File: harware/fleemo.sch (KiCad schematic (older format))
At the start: 33 parts, among them P1 CONN_01X02, Q1 STD2HNK60Z-1

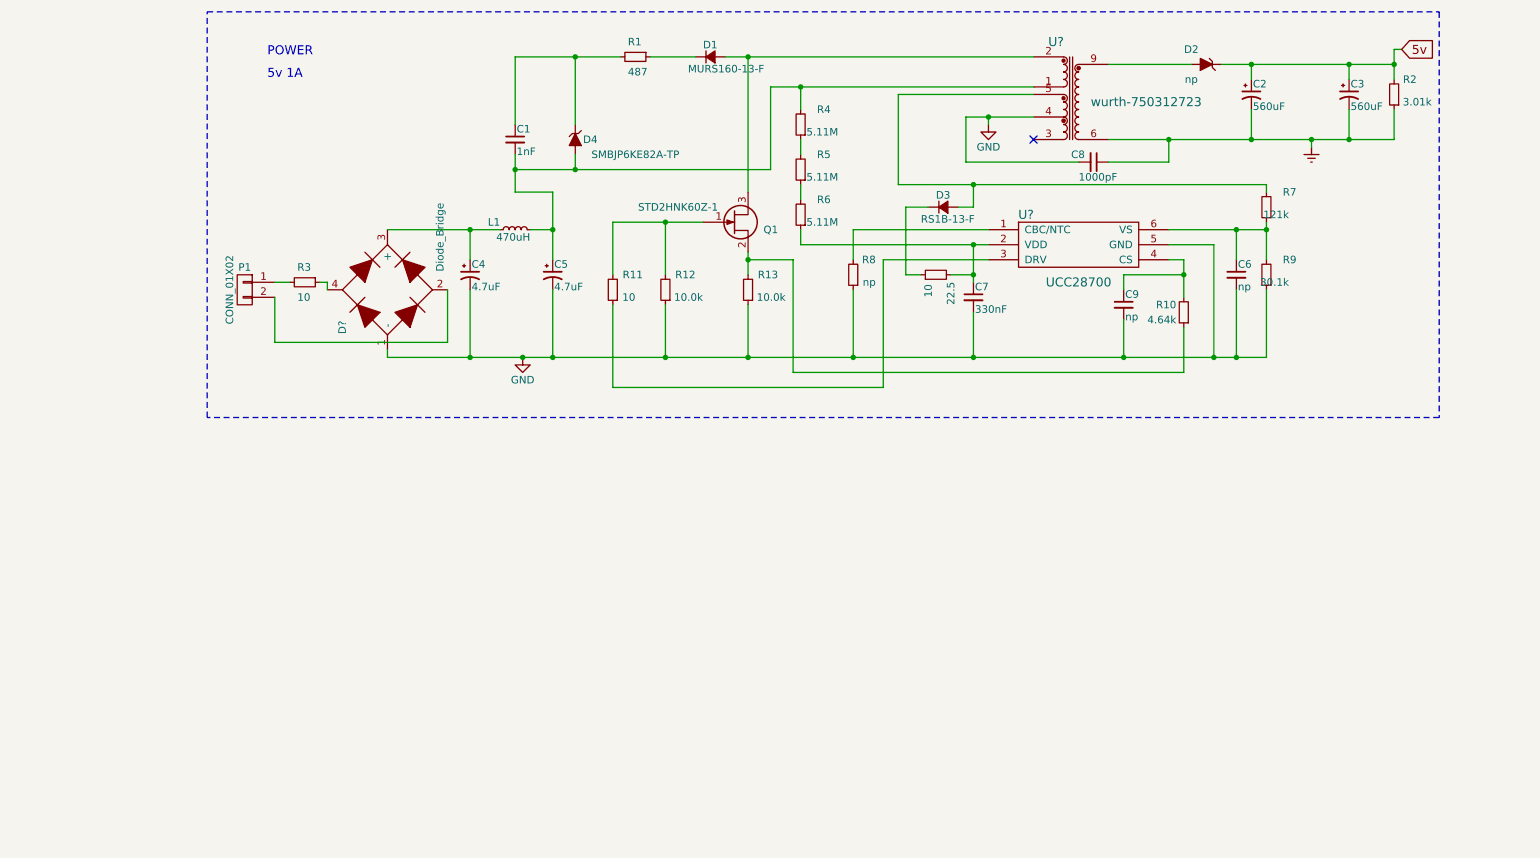
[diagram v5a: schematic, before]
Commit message: add stepdown circuit
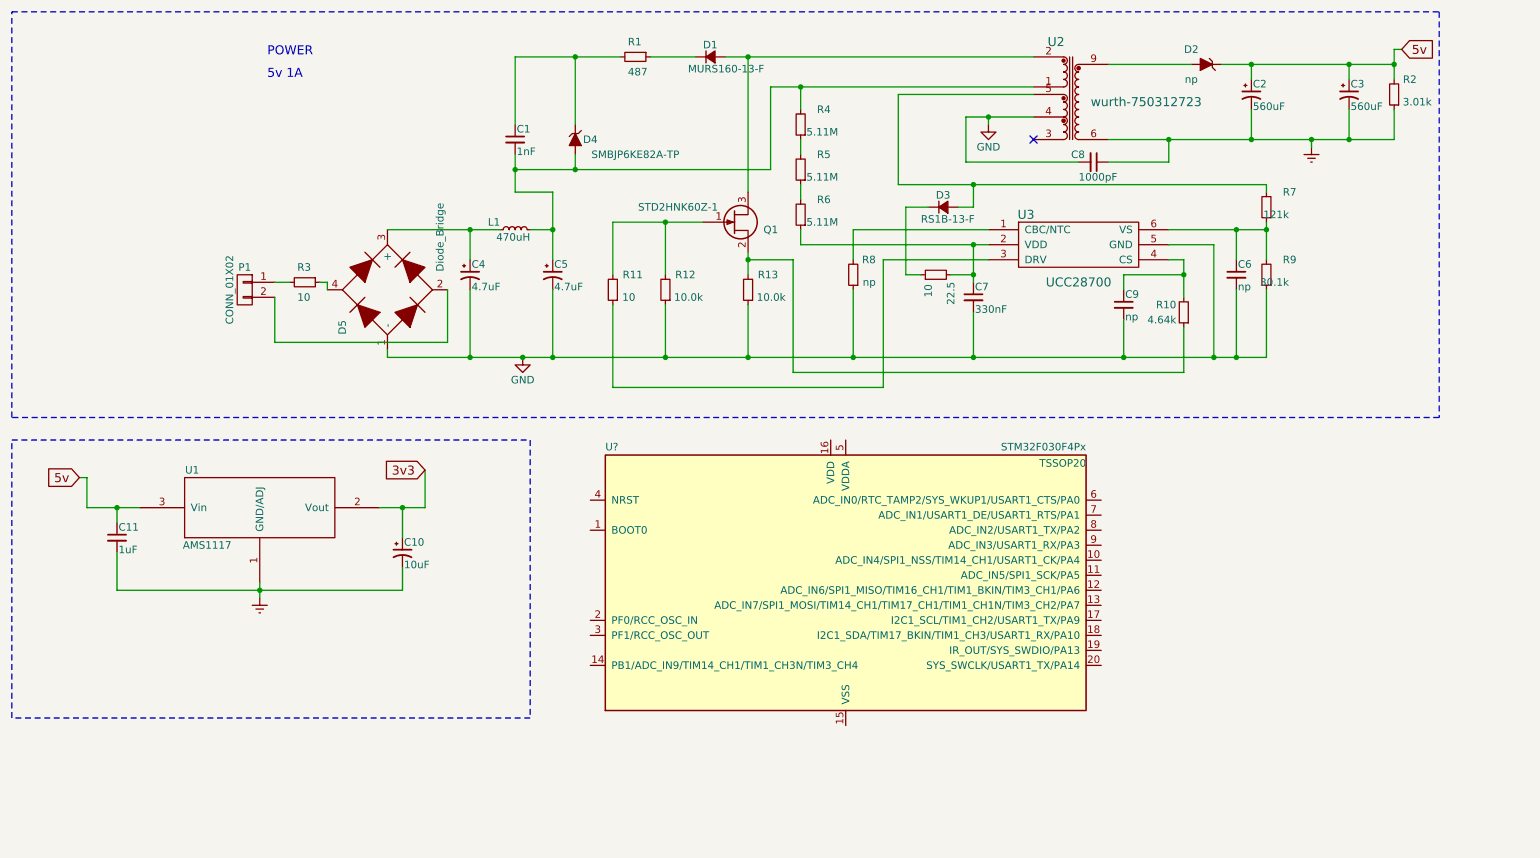
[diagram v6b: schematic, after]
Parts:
- added C10: 10uF, symbol CP1_Small
- added C11: 1uF, symbol C_Small
- added U1: AMS1117, symbol AMS1117
- added U?: STM32F030F4Px, TSSOP20, symbol STM32F030F4Px
- gave numbers to parts that had none: 3
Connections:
- net 5v: now also C11.1, U1.3 (Vin)
- net Earth: now also C10.2, C11.2, U1.1 (GND/ADJ)
- new net 3v3: C10.1, U1.2 (Vout)
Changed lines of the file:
@@
 LIBS:wurth-750312723
 LIBS:UCC28700
+LIBS:stm32
+LIBS:Power_Management
+LIBS:AMS1117
 LIBS:fleemo-cache
 EELAYER 25 0
@@
 $EndComp
 $Comp
-L GND #PWR01
+L GND #PWR2
 U 1 1 578589FE
 P 4500 3100
-F 0 "#PWR01" H 4500 2850 50  0001 C CNN
+F 0 "#PWR2" H 4500 2850 50  0001 C CNN
 F 1 "GND" H 4500 2950 50  0000 C CNN
 F 2 "" H 4500 3100 50  0000 C CNN
@@
 $EndComp
 $Comp
-L Earth #PWR05
+L Earth #PWR4
 U 1 1 578722E6
 P 9750 1700
-F 0 "#PWR05" H 9750 1450 50  0001 C CNN
+F 0 "#PWR4" H 9750 1450 50  0001 C CNN
 F 1 "Earth" H 9750 1550 50  0001 C CNN
 F 2 "" H 9750 1700 50  0000 C CNN
@@
 $EndComp
 $Comp
-L wurth-750312723 U?
+L wurth-750312723 U2
 U 1 1 578D71AD
 P 8150 1900
-F 0 "U?" H 8050 2800 60  0000 C CNN
+F 0 "U2" H 8050 2800 60  0000 C CNN
 F 1 "wurth-750312723" H 8650 2400 60  0000 C CNN
 F 2 "" H 8150 1900 60  0000 C CNN
@@
 $EndComp
 $Comp
-L UCC28700 U?
+L UCC28700 U3
 U 1 1 578EB042
 P 8200 2600
-F 0 "U?" H 7850 3050 60  0000 C CNN
+F 0 "U3" H 7850 3050 60  0000 C CNN
 F 1 "UCC28700" H 8200 2600 60  0000 C CNN
 F 2 "" H 8200 2600 60  0000 C CNN
@@
 $EndComp
 $Comp
-L GND #PWR?
+L GND #PWR3
 U 1 1 578EBE22
 P 7600 1550
-F 0 "#PWR?" H 7600 1300 50  0001 C CNN
+F 0 "#PWR3" H 7600 1300 50  0001 C CNN
 F 1 "GND" H 7600 1400 50  0000 C CNN
 F 2 "" H 7600 1550 50  0000 C CNN
@@
 	4700 3100 4700 2650
 Wire Wire Line
-	5100 2200 5450 2200
-Wire Wire Line
-	5450 2200 5700 2200
+	5100 2200 5700 2200
 Connection ~ 4500 3100
 Wire Wire Line
@@
 	4150 2250 4150 2450
 Wire Wire Line
-	4700 2000 4700 2250
-Wire Wire Line
-	4700 2250 4700 2450
+	4700 2000 4700 2450
 Wire Wire Line
 	4700 2250 4550 2250
@@
 	4450 2000 4700 2000
 Wire Wire Line
-	4450 1750 4450 1850
-Wire Wire Line
-	4450 1850 4450 2000
+	4450 1750 4450 2000
 Wire Wire Line
 	4450 1550 4450 1100
 Wire Wire Line
-	4450 1100 4850 1100
-Wire Wire Line
-	4850 1100 5150 1100
-Wire Wire Line
-	4450 1850 4850 1850
-Wire Wire Line
-	4850 1850 6150 1850
+	4450 1100 5150 1100
+Wire Wire Line
+	4450 1850 6150 1850
 Wire Wire Line
 	4850 1850 4850 1750
@@
 	5350 1100 5650 1100
 Wire Wire Line
-	5850 1100 6000 1100
-Wire Wire Line
-	6000 1100 7900 1100
+	5850 1100 7900 1100
 Wire Wire Line
 	6000 1100 6000 2000
@@
 	5450 2550 5450 2200
 Wire Wire Line
-	6000 2400 6000 2450
-Wire Wire Line
-	6000 2450 6000 2550
+	6000 2400 6000 2550
 Wire Wire Line
 	6000 3100 6000 2750
@@
 	6350 1450 6350 1300
 Wire Wire Line
-	6150 1300 6350 1300
-Wire Wire Line
-	6350 1300 7900 1300
+	6150 1300 7900 1300
 Wire Wire Line
 	6350 1650 6350 1750
@@
 	6350 2250 6350 2350
 Wire Wire Line
-	6350 2350 7500 2350
-Wire Wire Line
-	7500 2350 7600 2350
+	6350 2350 7600 2350
 Wire Wire Line
 	5100 2550 5100 2200
@@
 	7000 1350 7000 1950
 Wire Wire Line
-	7000 1950 7500 1950
-Wire Wire Line
-	7500 1950 9450 1950
+	7000 1950 9450 1950
 Wire Wire Line
 	9450 1950 9450 2000
 Wire Wire Line
-	9450 2200 9450 2250
-Wire Wire Line
-	9450 2250 9450 2450
+	9450 2200 9450 2450
 Wire Wire Line
 	9450 3100 9450 2650
@@
 $EndComp
 Wire Wire Line
-	7500 2350 7500 2550
-Wire Wire Line
-	7500 2550 7500 2600
+	7500 2350 7500 2600
 Connection ~ 7500 2350
 Wire Wire Line
@@
 Connection ~ 7500 1950
 Wire Wire Line
-	8800 2250 9250 2250
-Wire Wire Line
-	9250 2250 9450 2250
+	8800 2250 9450 2250
 Connection ~ 9450 2250
 $Comp
@@
 	8800 2450 8900 2450
 Wire Wire Line
-	8900 2450 8900 2550
-Wire Wire Line
-	8900 2550 8900 2700
+	8900 2450 8900 2700
 Wire Wire Line
 	8900 2900 8900 3200
@@
 	8800 2350 9100 2350
 Wire Wire Line
-	9100 2350 9100 3100
+	9100 3100 9100 2350
 Connection ~ 9100 3100
 $Comp
@@
 $EndComp
 Wire Wire Line
-	9150 1150 9350 1150
-Wire Wire Line
-	9350 1150 10000 1150
-Wire Wire Line
-	10000 1150 10300 1150
+	9150 1150 10300 1150
 Wire Wire Line
 	9350 1150 9350 1250
 Wire Wire Line
-	8400 1650 8800 1650
-Wire Wire Line
-	8800 1650 9350 1650
-Wire Wire Line
-	9350 1650 9750 1650
-Wire Wire Line
-	9750 1650 10000 1650
-Wire Wire Line
-	10000 1650 10300 1650
+	8400 1650 10300 1650
 Wire Wire Line
 	9350 1650 9350 1450
@@
 $EndComp
 Wire Wire Line
-	10300 1050 10300 1150
-Wire Wire Line
-	10300 1150 10300 1250
+	10300 1050 10300 1250
 Connection ~ 10000 1150
 Wire Wire Line
@@
 $EndComp
 Wire Wire Line
-	7900 1500 7600 1500
-Wire Wire Line
-	7600 1500 7450 1500
+	7450 1500 7900 1500
 Wire Wire Line
 	7450 1500 7450 1800
@@
 NoConn ~ 7900 1650
 $Comp
-L Diode_Bridge D?
+L Diode_Bridge D5
 U 1 1 578EFF8B
 P 3600 2650
-F 0 "D?" H 3350 2950 50  0000 C CNN
+F 0 "D5" H 3350 2950 50  0000 C CNN
 F 1 "Diode_Bridge" H 3950 2300 50  0000 C CNN
 F 2 "" H 3600 2650 50  0000 C CNN
@@
 $EndComp
 Wire Wire Line
-	3600 2250 4150 2250
-Wire Wire Line
-	4150 2250 4350 2250
-Wire Wire Line
-	3600 3100 4150 3100
-Wire Wire Line
-	4150 3100 4500 3100
-Wire Wire Line
-	4500 3100 4700 3100
-Wire Wire Line
-	4700 3100 5450 3100
-Wire Wire Line
-	5450 3100 6000 3100
-Wire Wire Line
-	6000 3100 6700 3100
-Wire Wire Line
-	6700 3100 7500 3100
-Wire Wire Line
-	7500 3100 8500 3100
-Wire Wire Line
-	8500 3100 9100 3100
-Wire Wire Line
-	9100 3100 9250 3100
-Wire Wire Line
-	9250 3100 9450 3100
+	3600 2250 4350 2250
+Wire Wire Line
+	3600 3100 9450 3100
 Wire Wire Line
 	3600 3100 3600 3050
@@
 Connection ~ 10300 1150
 Wire Notes Line
-	2400 800  10600 800
+	1100 800  10600 800
 Wire Notes Line
 	10600 800  10600 3500
 Wire Notes Line
-	10600 3500 2400 3500
+	10600 3500 1100 3500
 Wire Notes Line
-	2400 3500 2400 800
+	1100 3500 1100 800
 Text Notes 2800 1100 0    60   ~ 0
 POWER
 Text Notes 2800 1250 0    60   ~ 0
 5v 1A\n
+$Comp
+L AMS1117 U1
+U 1 1 579014E8
+P 2750 4100
+F 0 "U1" H 2300 4350 50  0000 C CNN
+F 1 "AMS1117" H 2400 3850 50  0000 C CNN
+F 2 "" H 2750 4100 60  0000 C CNN
+F 3 "" H 2750 4100 60  0000 C CNN
+	1    2750 4100
+	1    0    0    -1
+$EndComp
+Text GLabel 1550 3900 0    60   Input ~ 0
+5v
+Wire Wire Line
+	1550 3900 1600 3900
+Wire Wire Line
+	1600 3900 1600 4100
+Wire Wire Line
+	1600 4100 1950 4100
+$Comp
+L Earth #PWR1
+U 1 1 57901AFF
+P 2750 4700
+F 0 "#PWR1" H 2750 4450 50  0001 C CNN
+F 1 "Earth" H 2750 4550 50  0001 C CNN
+F 2 "" H 2750 4700 50  0000 C CNN
+F 3 "" H 2750 4700 50  0000 C CNN
+	1    2750 4700
+	1    0    0    -1
+$EndComp
+Wire Wire Line
+	2750 4600 2750 4700
+Text GLabel 3850 3850 0    60   Input ~ 0
+3v3
+Wire Wire Line
+	3550 4100 3850 4100
+Wire Wire Line
+	3850 4100 3850 3850
+$Comp
+L CP1_Small C10
+U 1 1 5790220C
+P 3700 4400
+F 0 "C10" H 3710 4470 50  0000 L CNN
+F 1 "10uF" H 3710 4320 50  0000 L CNN
+F 2 "" H 3700 4400 50  0000 C CNN
+F 3 "" H 3700 4400 50  0000 C CNN
+	1    3700 4400
+	1    0    0    -1
+$EndComp
+Wire Wire Line
+	3700 4300 3700 4100
+Connection ~ 3700 4100
+Wire Wire Line
+	3700 4650 3700 4500
+Wire Wire Line
+	1800 4650 3700 4650
+Connection ~ 2750 4650
+$Comp
+L C_Small C11
+U 1 1 579028FD
+P 1800 4300
+F 0 "C11" H 1810 4370 50  0000 L CNN
+F 1 "1uF" H 1810 4220 50  0000 L CNN
+F 2 "" H 1800 4300 50  0000 C CNN
+F 3 "" H 1800 4300 50  0000 C CNN
+	1    1800 4300
+	1    0    0    -1
+$EndComp
+Wire Wire Line
+	1800 4200 1800 4100
+Connection ~ 1800 4100
+Wire Wire Line
+	1800 4400 1800 4650
+Wire Notes Line
+	1100 3650 4550 3650
+Wire Notes Line
+	4550 3650 4550 5500
+Wire Notes Line
+	4550 5500 1100 5500
+Wire Notes Line
+	1100 5500 1100 3650
+$Comp
+L STM32F030F4Px U?
+U 1 1 57903FF1
+P 6650 4650
+F 0 "U?" H 5050 5575 50  0000 L BNN
+F 1 "STM32F030F4Px" H 8250 5575 50  0000 R BNN
+F 2 "TSSOP20" H 8250 5525 50  0000 R TNN
+F 3 "" H 6650 4650 50  0000 C CNN
+	1    6650 4650
+	1    0    0    -1
+$EndComp
 $EndSCHEMATC

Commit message: add mcu circuit
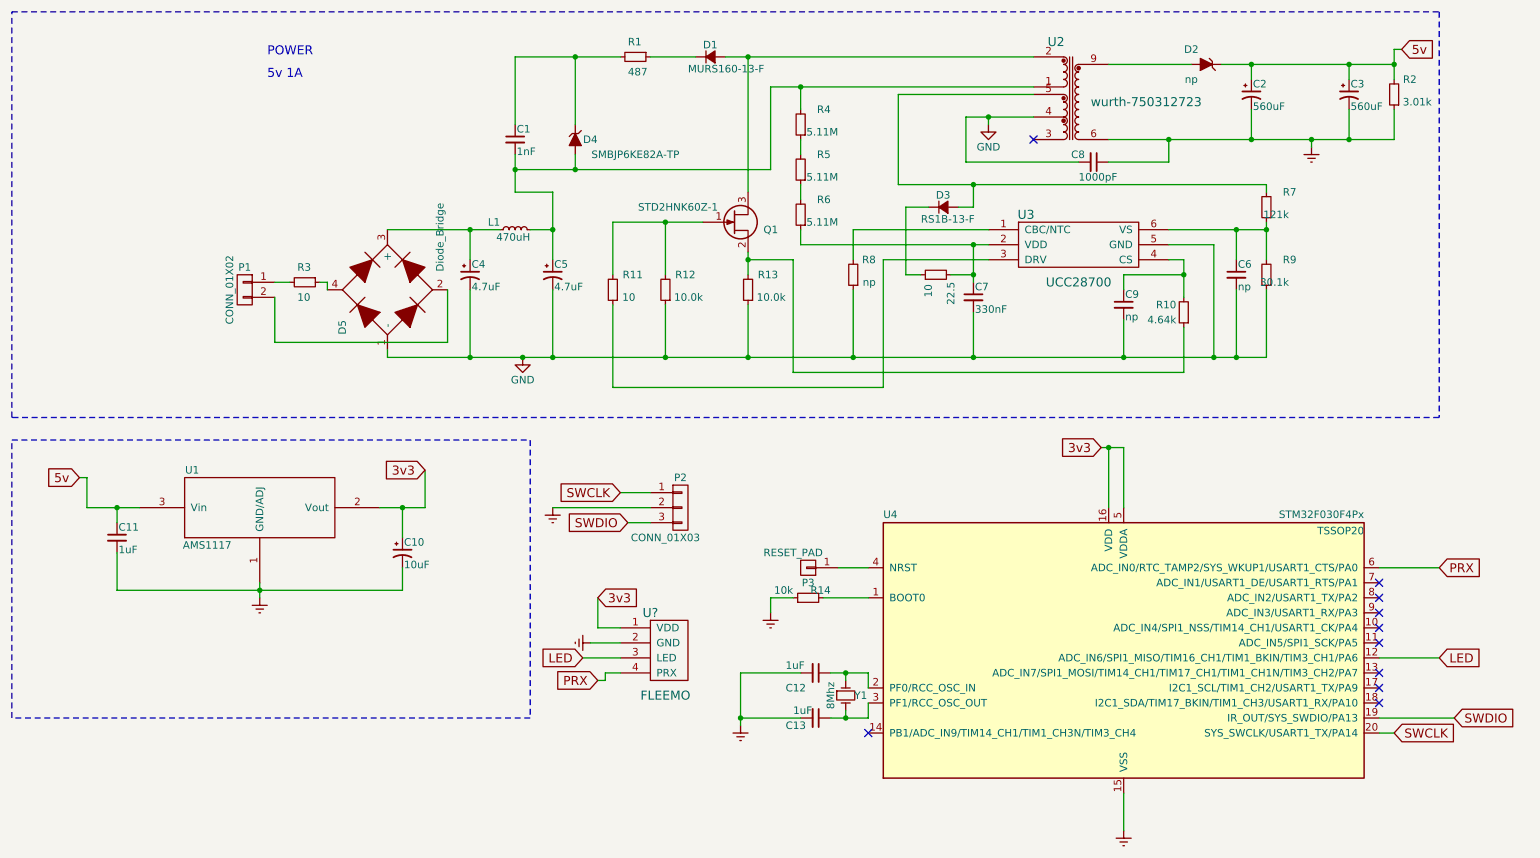
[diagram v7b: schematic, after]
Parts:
- added C12, C13: 1uF, symbol C_Small
- added P2: CONN_01X03, symbol CONN_01X03
- added P3: RESET_PAD, symbol CONN_01X01
- added R14: 10k, symbol R_Small
- added U?: FLEEMO, symbol FLEEMO
- added Y1: 8Mhz, symbol Crystal_Small
- gave numbers to parts that had none: 1
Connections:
- net 3v3: now also U4.16 (VDD), U4.5 (VDDA), U?.1 (VDD)
- net Earth: now also U4.15 (VSS), C12.2, C13.2, P2.2 (P2), R14.1, U?.2 (GND)
- net at U4.1 (BOOT0): now also R14.2
- net LED: now reaches U4.12 (ADC_IN6/SPI1_MISO/TIM16_CH1/TIM1_BKIN/TIM3_CH1/PA6)
- net LED: now also U?.3 (LED)
- net SWDIO: now reaches U4.19 (IR_OUT/SYS_SWDIO/PA13)
- net SWDIO: now also P2.3 (P3)
- net at U4.2 (PF0/RCC_OSC_IN): now also C12.1, Y1.1
- net SWCLK: now reaches U4.20 (SYS_SWCLK/USART1_TX/PA14)
- net SWCLK: now also P2.1 (P1)
- net at U4.3 (PF1/RCC_OSC_OUT): now also C13.1, Y1.2
- net at U4.4 (NRST): now also P3.1 (P1)
- net PRX: now reaches U4.6 (ADC_IN0/RTC_TAMP2/SYS_WKUP1/USART1_CTS/PA0)
- net PRX: now also U?.4 (PRX)
- no-connect marks 1 -> 10
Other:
- moved on the sheet: U4

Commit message: add footprint
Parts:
- added C14: 100nF, Capacitors_SMD:C_0805_HandSoldering, symbol C_Small
- added C15: 4.7uF, Capacitors_SMD:C_0805_HandSoldering, symbol C_Small
- added C16: 1uF, Capacitors_Tantalum_SMD:TantalC_SizeA_EIA-3216_HandSoldering, symbol CP1_Small
- added C17: 10nF, Capacitors_SMD:C_0805_HandSoldering, symbol C_Small
- C1: footprint (none) -> Capacitors_SMD:C_1206_HandSoldering
- C10: footprint (none) -> Capacitors_Tantalum_SMD:TantalC_SizeA_EIA-3216_HandSoldering
- C11, C6, C7, C9: footprint (none) -> Capacitors_SMD:C_0805_HandSoldering
- C12, C13: value 1uF -> 22pF; footprint (none) -> Capacitors_SMD:C_0805_HandSoldering
- C2, C3: footprint (none) -> Capacitors_ThroughHole:C_Radial_D10_L13_P5
- C4, C5: footprint (none) -> Capacitors_ThroughHole:C_Radial_D10_L16_P5
- C8: footprint (none) -> Capacitors_ThroughHole:C_Rect_L13_W4_P10
- D1: footprint (none) -> Diodes_ThroughHole:Diode_DO-41_SOD81_Horizontal_RM10
- D2: value np -> B340LB-13-F; footprint (none) -> Diodes_SMD:SMB_Handsoldering
- D3: footprint (none) -> Diodes_SMD:SMA_Handsoldering
- D4: footprint (none) -> Diodes_SMD:SMB_Handsoldering
- D5: footprint (none) -> lib:diode_bridge
- L1: footprint (none) -> lib:choke_F_2mm
- Q1: footprint (none) -> TO_SOT_Packages_THT:TO-251AA
- R1, R10, R11, R12, R2, R4, R5, R6, R7, R8, R9: footprint (none) -> Resistors_SMD:R_0805_HandSoldering
- R13: footprint (none) -> Resistors_SMD:R_1206_HandSoldering
- R14: renamed from 22.5; value 10 -> 22.5; footprint (none) -> Resistors_SMD:R_0805_HandSoldering
- R15: renamed from R14; footprint (none) -> Resistors_SMD:R_0805_HandSoldering
- U1: footprint (none) -> lib:SOT-223
- U3: footprint (none) -> TO_SOT_Packages_SMD:SOT-23-6_Handsoldering
- Y1: footprint (none) -> Crystals:Crystal_HC49-SD_SMD
- gave numbers to parts that had none: 1
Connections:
- net 3v3: now also C14.2, C15.2, C16.1, C17.1
- net Earth: now also C14.1, C15.1, C16.2, C17.2
